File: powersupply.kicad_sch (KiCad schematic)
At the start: 0 parts

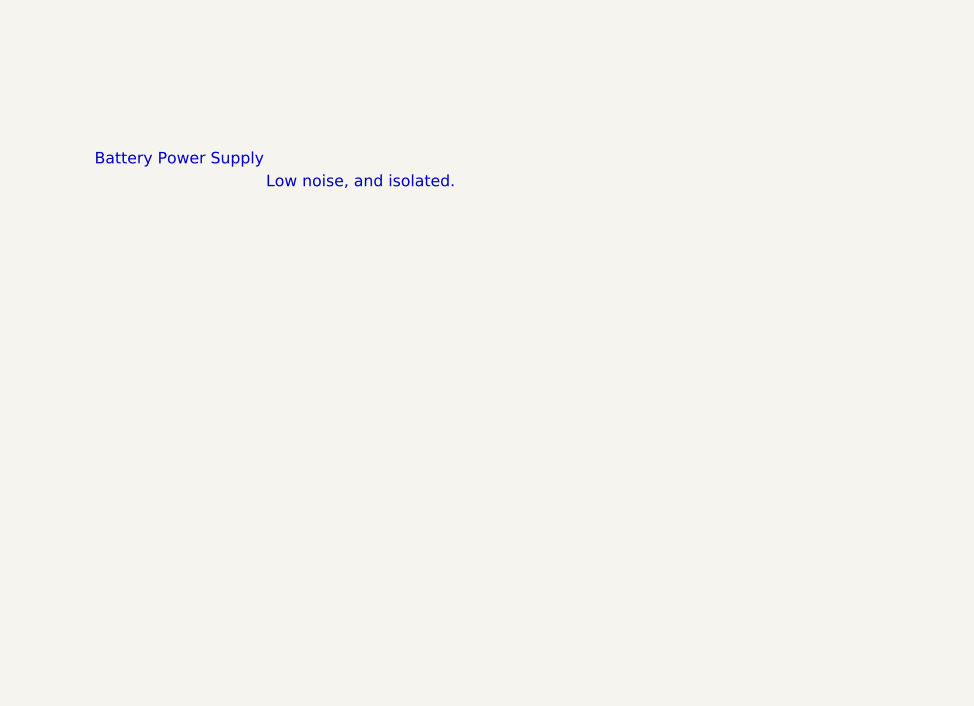
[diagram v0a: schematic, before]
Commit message: added 3 linear regulators
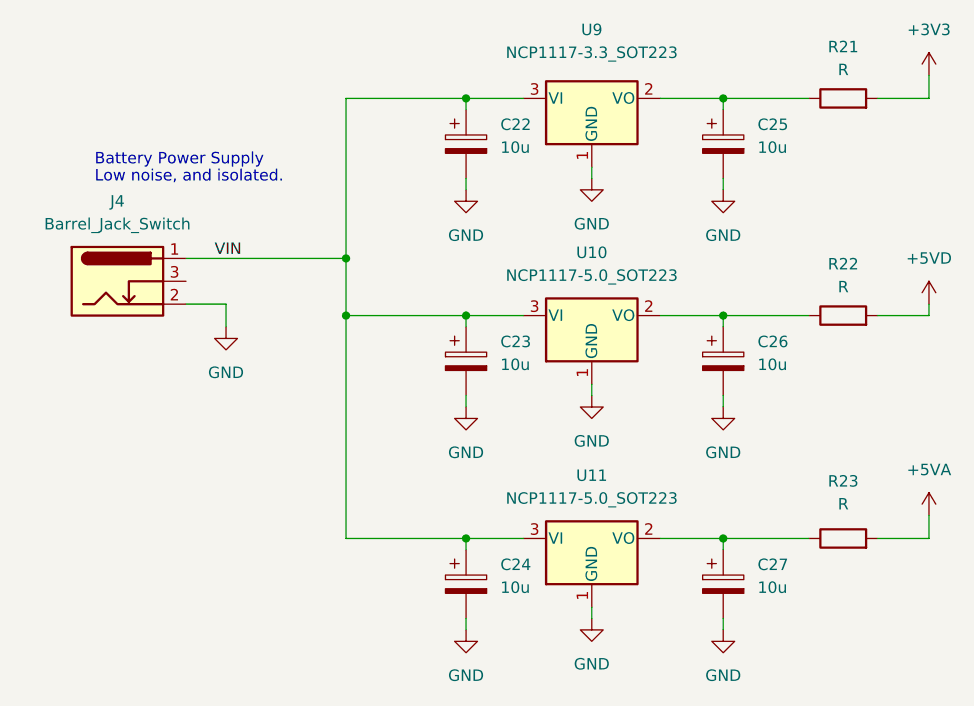
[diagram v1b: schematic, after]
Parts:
- added C22, C23, C24, C25, C26, C27: 10u, Capacitor_SMD:CP_Elec_4x3.9, symbol Device:C_Polarized
- added J4: Barrel_Jack_Switch, Connector_BarrelJack:BarrelJack_Wuerth_6941xx301002, symbol Connector:Barrel_Jack_Switch
- added R21, R22, R23: R, Resistor_SMD:R_0603_1608Metric, symbol Device:R
- added U10, U11: NCP1117-5.0_SOT223, Package_TO_SOT_SMD:SOT-223-3_TabPin2, symbol Regulator_Linear:NCP1117-5.0_SOT223
- added U9: NCP1117-3.3_SOT223, Package_TO_SOT_SMD:SOT-223-3_TabPin2, symbol Regulator_Linear:NCP1117-3.3_SOT223
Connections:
- new net: C25.1, R21.1, U9.2 (VO)
- new net: C26.1, R22.1, U10.2 (VO)
- new net: C27.1, R23.1, U11.2 (VO)
- new net +3V3: R21.2
- new net +5VA: R23.2
- new net +5VD: R22.2
- new net GND: C22.2, C23.2, C24.2, C25.2, C26.2, C27.2, J4.2, U10.1 (GND), U11.1 (GND), U9.1 (GND)
- new net VIN: C22.1, C23.1, C24.1, J4.1, U10.3 (VI), U11.3 (VI), U9.3 (VI)
